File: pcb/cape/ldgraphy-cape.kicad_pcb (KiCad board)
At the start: 2 copper layers, 35.1 x 49.5 mm, 27 parts, among them J1 CONN_01X03, P2 PhDiode, P3 Jumper, P4 BaseConn, P5 CONN_01X05, P6 12V-in, P9 BB_P9, U1 POLOLUSTEPPER, U2 DCDC1584, U3 MIC920, U4 MIC920

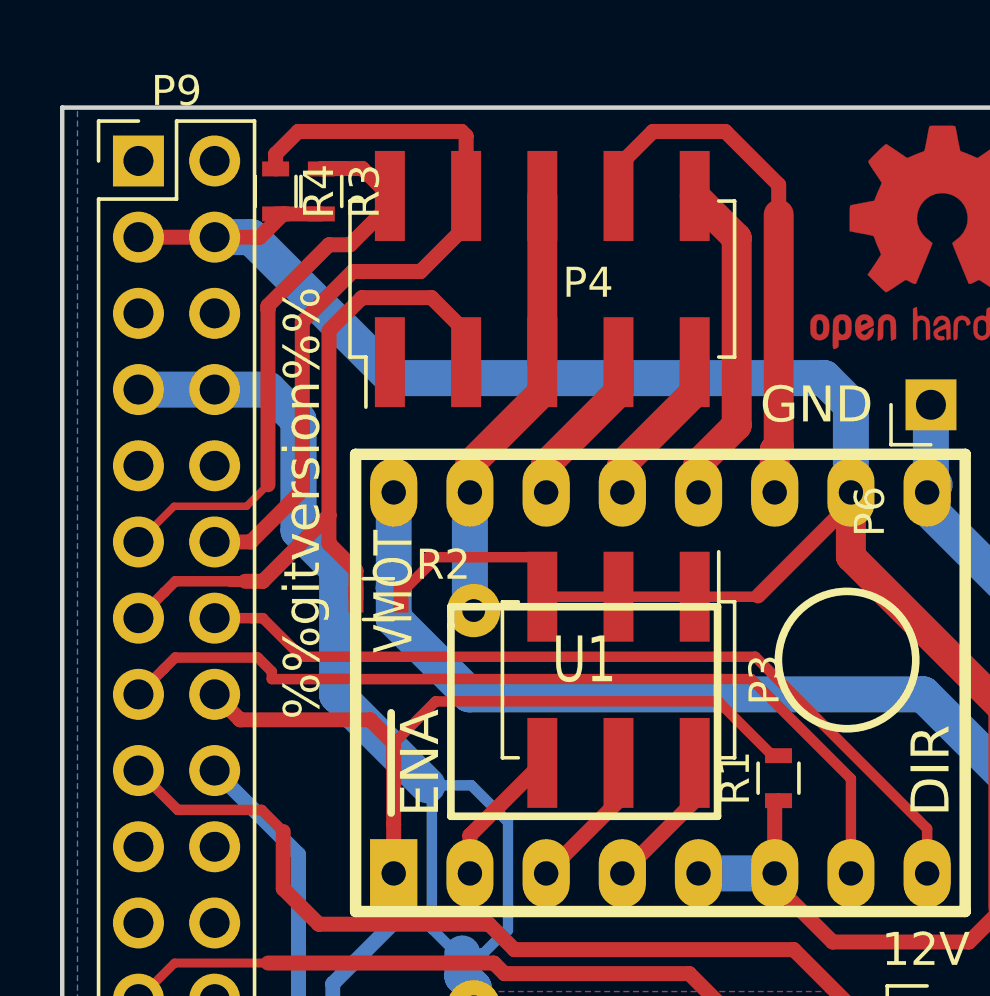
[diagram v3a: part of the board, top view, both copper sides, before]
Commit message: o Update values in schematics.
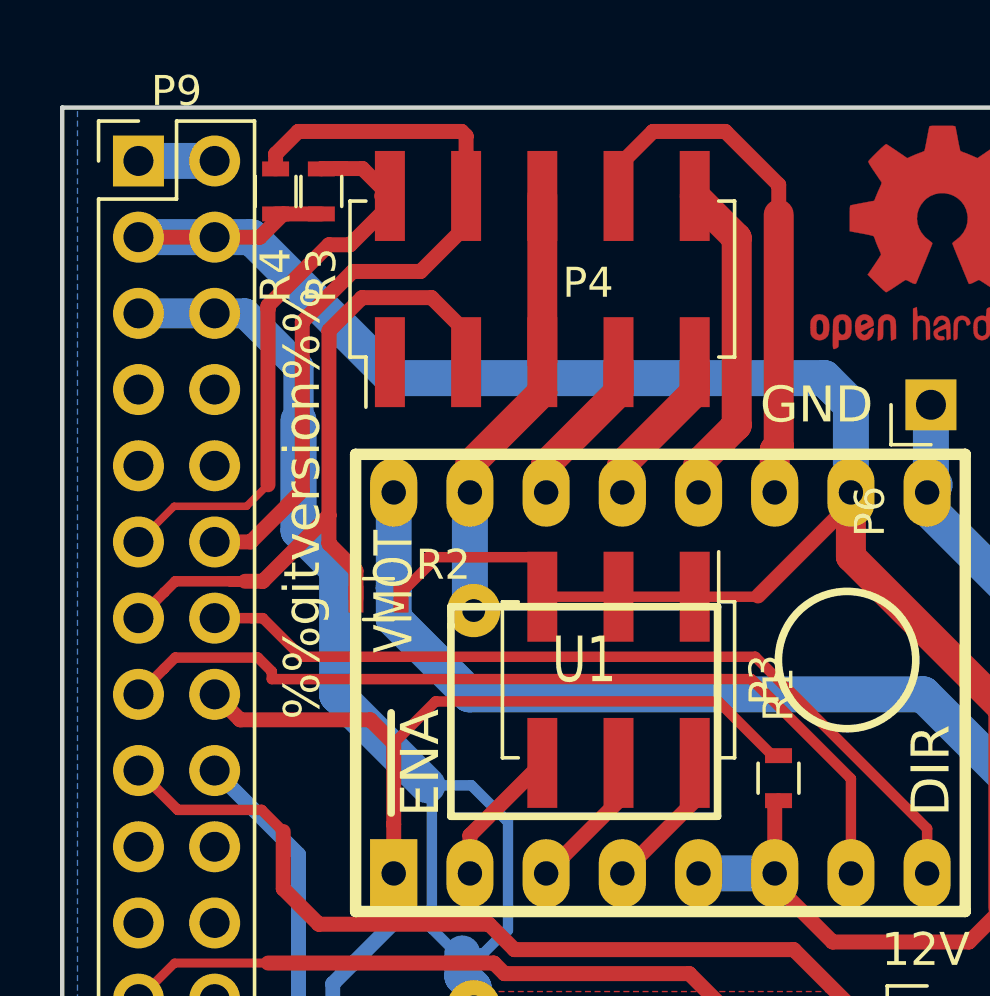
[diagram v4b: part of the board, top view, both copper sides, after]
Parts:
- R10, R13, R15: value R -> 8k2
- R11, R14, R9: value R -> 22k
- R12: value 1k -> 1k5
- R16: value 2k2 -> 8k2
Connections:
- P9 pad 5: (no net) -> +5V
- P9 pad 6: (no net) -> +5V
- P9 pad 7: +5V -> (no net)
- P9 pad 8: +5V -> (no net)
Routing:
- net GND: track 50.1 -> 52.6 mm
- net 3.3V: track 82.5 -> 85.1 mm
- net +5V: track 57.2 -> 59.3 mm
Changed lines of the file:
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@@
   (general
     (links 74)
-    (no_connects 0)
+    (no_connects 2)
     (area 69.774999 41.3705 114.004286 102.945001)
     (thickness 1.6)
     (drawings 17)
-    (tracks 278)
+    (tracks 281)
     (zones 0)
     (modules 27)
@@
     (pad 1 smd rect (at -2.77 -2.54 270) (size 3 1) (layers F.Cu F.Paste F.Mask)
       (net 5 3.3V))
-    (model ${KISYS3DMOD}/Pin_Headers.3dshapes/Pin_Header_Straight_2x03_Pitch2.54mm_SMD.wrl
-      (at (xyz 0 0 0))
-      (scale (xyz 1 1 1))
-      (rotate (xyz 0 0 0))
-    )
   )
   (module TO_SOT_Packages_SMD:SOT-353_SC-70-5 (layer F.Cu)
@@
     (pad 1 smd rect (at -0.95 -0.65 90) (size 0.65 0.4) (layers F.Cu F.Paste F.Mask)
       (net 15 "Net-(R13-Pad1)"))
-    (model ${KISYS3DMOD}/TO_SOT_Packages_SMD.3dshapes/SOT-353_SC-70-5.wrl
+    (model ${KISYS3DMOD}/TO_SOT_Packages_SMD.3dshapes/SC-70-5.wrl
       (at (xyz 0 0 0))
       (scale (xyz 1 1 1))
-      (rotate (xyz 0 0 0))
+      (rotate (xyz 0 0 90))
     )
   )
@@
     (pad 1 smd rect (at -0.95 -0.65 90) (size 0.65 0.4) (layers F.Cu F.Paste F.Mask)
       (net 16 "Net-(R10-Pad2)"))
-    (model ${KISYS3DMOD}/TO_SOT_Packages_SMD.3dshapes/SOT-353_SC-70-5.wrl
+    (model ${KISYS3DMOD}/TO_SOT_Packages_SMD.3dshapes/SC-70-5.wrl
       (at (xyz 0 0 0))
       (scale (xyz 1 1 1))
-      (rotate (xyz 0 0 0))
+      (rotate (xyz 0 0 90))
     )
   )
@@
       (effects (font (size 1 1) (thickness 0.15)))
     )
-    (fp_text value R (at 0 1.5 270) (layer F.Fab)
+    (fp_text value 22k (at 0 1.5 270) (layer F.Fab)
       (effects (font (size 1 1) (thickness 0.15)))
     )
@@
       (effects (font (size 1 1) (thickness 0.15)))
     )
-    (fp_text value R (at 0 1.5 270) (layer F.Fab)
+    (fp_text value 8k2 (at 0 1.5 270) (layer F.Fab)
       (effects (font (size 1 1) (thickness 0.15)))
     )
@@
       (effects (font (size 1 1) (thickness 0.15)))
     )
-    (fp_text value R (at 0 1.5 270) (layer F.Fab)
+    (fp_text value 22k (at 0 1.5 270) (layer F.Fab)
       (effects (font (size 1 1) (thickness 0.15)))
     )
@@
       (effects (font (size 1 1) (thickness 0.15)))
     )
-    (fp_text value 1k (at 0 1.5 90) (layer F.Fab)
+    (fp_text value 1k5 (at 0 1.5 90) (layer F.Fab)
       (effects (font (size 1 1) (thickness 0.15)))
     )
@@
       (effects (font (size 1 1) (thickness 0.15)))
     )
-    (fp_text value R (at 0 1.5 270) (layer F.Fab)
+    (fp_text value 8k2 (at 0 1.5 270) (layer F.Fab)
       (effects (font (size 1 1) (thickness 0.15)))
     )
@@
       (effects (font (size 1 1) (thickness 0.15)))
     )
-    (fp_text value R (at 0 1.5 270) (layer F.Fab)
+    (fp_text value 22k (at 0 1.5 270) (layer F.Fab)
       (effects (font (size 1 1) (thickness 0.15)))
     )
@@
       (effects (font (size 1 1) (thickness 0.15)))
     )
-    (fp_text value R (at 0 1.5 270) (layer F.Fab)
+    (fp_text value 8k2 (at 0 1.5 270) (layer F.Fab)
       (effects (font (size 1 1) (thickness 0.15)))
     )
@@
       (effects (font (size 1 1) (thickness 0.15)))
     )
-    (fp_text value 2k2 (at 0 1.5 180) (layer F.Fab)
+    (fp_text value 8k2 (at 0 1.5 180) (layer F.Fab)
       (effects (font (size 1 1) (thickness 0.15)))
     )
@@
     (tags "resistor 0603")
     (attr smd)
-    (fp_text reference R1 (at 0 -1.45 90) (layer F.SilkS)
+    (fp_text reference R1 (at 2.794 0 90) (layer F.SilkS)
       (effects (font (size 1 1) (thickness 0.15)))
     )
@@
     (tags "resistor 0603")
     (attr smd)
-    (fp_text reference R3 (at 0 -1.45 270) (layer F.SilkS)
+    (fp_text reference R3 (at 2.794 0 270) (layer F.SilkS)
       (effects (font (size 1 1) (thickness 0.15)))
     )
@@
       (net 25 ~UI-Button))
     (pad 1 smd rect (at -2.77 -5.08 90) (size 3 1) (layers F.Cu F.Paste F.Mask))
-    (model ${KISYS3DMOD}/Pin_Headers.3dshapes/Pin_Header_Straight_2x05_Pitch2.54mm_SMD.wrl
+    (model ${KISYS3DMOD}/Pin_Headers.3dshapes/Pin_Header_Straight_2x05_Pitch2.54mm.wrl
       (at (xyz 0 0 0))
       (scale (xyz 1 1 1))
-      (rotate (xyz 0 0 0))
+      (rotate (xyz 0 0 90))
     )
   )
@@
     (tags "resistor 0603")
     (attr smd)
-    (fp_text reference R4 (at 0 -1.45 270) (layer F.SilkS)
+    (fp_text reference R4 (at 2.794 0 270) (layer F.SilkS)
       (effects (font (size 1 1) (thickness 0.15)))
     )
@@
     (pad 10 thru_hole oval (at 2.54 10.16) (size 1.7 1.7) (drill 1) (layers *.Cu *.Mask))
     (pad 9 thru_hole oval (at 0 10.16) (size 1.7 1.7) (drill 1) (layers *.Cu *.Mask))
-    (pad 8 thru_hole oval (at 2.54 7.62) (size 1.7 1.7) (drill 1) (layers *.Cu *.Mask)
+    (pad 8 thru_hole oval (at 2.54 7.62) (size 1.7 1.7) (drill 1) (layers *.Cu *.Mask))
+    (pad 7 thru_hole oval (at 0 7.62) (size 1.7 1.7) (drill 1) (layers *.Cu *.Mask))
+    (pad 6 thru_hole oval (at 2.54 5.08) (size 1.7 1.7) (drill 1) (layers *.Cu *.Mask)
       (net 8 +5V))
-    (pad 7 thru_hole oval (at 0 7.62) (size 1.7 1.7) (drill 1) (layers *.Cu *.Mask)
+    (pad 5 thru_hole oval (at 0 5.08) (size 1.7 1.7) (drill 1) (layers *.Cu *.Mask)
       (net 8 +5V))
-    (pad 6 thru_hole oval (at 2.54 5.08) (size 1.7 1.7) (drill 1) (layers *.Cu *.Mask))
-    (pad 5 thru_hole oval (at 0 5.08) (size 1.7 1.7) (drill 1) (layers *.Cu *.Mask))
     (pad 4 thru_hole oval (at 2.54 2.54) (size 1.7 1.7) (drill 1) (layers *.Cu *.Mask)
       (net 5 3.3V))
@@
   (gr_line (start 106.68 43.18) (end 106.68 92.71) (layer Edge.Cuts) (width 0.15))
   (gr_line (start 71.628 43.18) (end 106.68 43.18) (layer Edge.Cuts) (width 0.15))
+  (segment (start 76.708 44.958) (end 74.168 44.958) (width 1.2) (layer B.Cu) (net 1))
   (segment (start 85.217 56.007) (end 85.217 59.817) (width 1.2) (layer B.Cu) (net 1))
   (segment (start 85.217 59.817) (end 85.344 59.944) (width 1.2) (layer B.Cu) (net 1))
@@
   (segment (start 81.161 86.36) (end 79.502 84.701) (width 0.5) (layer B.Cu) (net 4))
   (segment (start 82.5246 86.36) (end 82.677 86.36) (width 0.35) (layer F.Cu) (net 4))
+  (segment (start 76.708 47.498) (end 74.168 47.498) (width 1.2) (layer B.Cu) (net 5))
   (segment (start 97.917 56.007) (end 97.917 58.15) (width 1) (layer F.Cu) (net 5))
   (segment (start 97.917 58.15) (end 102.997 63.23) (width 1) (layer F.Cu) (net 5))
@@
   (segment (start 100.457 67.214) (end 94.728001 61.485001) (width 0.35) (layer F.Cu) (net 7))
   (segment (start 100.457 68.707) (end 100.457 67.214) (width 0.35) (layer F.Cu) (net 7))
+  (segment (start 76.708 50.038) (end 74.168 50.038) (width 1) (layer B.Cu) (net 8))
+  (segment (start 77.724 50.038) (end 76.708 50.038) (width 1) (layer B.Cu) (net 8))
+  (segment (start 79.502 51.816) (end 77.724 50.038) (width 1) (layer B.Cu) (net 8))
+  (segment (start 79.502 53.594) (end 79.502 51.816) (width 1) (layer B.Cu) (net 8))
   (segment (start 85.344 73.152) (end 85.344 74.409235) (width 1.2) (layer F.Cu) (net 8))
   (segment (start 85.344 74.409235) (end 87.274508 76.339743) (width 1.2) (layer F.Cu) (net 8))
@@
   (segment (start 83.804401 65.770401) (end 84.265754 65.770401) (width 0.35) (layer B.Cu) (net 8))
   (segment (start 84.963 72.136) (end 84.963 71.374) (width 1.2) (layer B.Cu) (net 8))
-  (segment (start 76.708 52.578) (end 74.168 52.578) (width 1.2) (layer B.Cu) (net 8))
   (segment (start 83.804401 65.770401) (end 80.78959 62.75559) (width 1.2) (layer B.Cu) (net 8))
-  (segment (start 79.502 53.594) (end 78.486 52.578) (width 1.2) (layer B.Cu) (net 8))
   (segment (start 80.78959 62.75559) (end 80.78959 58.56459) (width 1.2) (layer B.Cu) (net 8))
   (segment (start 80.78959 58.56459) (end 79.502 57.277) (width 1.2) (layer B.Cu) (net 8))
   (segment (start 79.502 57.277) (end 79.502 53.594) (width 1.2) (layer B.Cu) (net 8))
-  (segment (start 78.486 52.578) (end 76.708 52.578) (width 1.2) (layer B.Cu) (net 8))
   (segment (start 88.60854 76.479508) (end 87.274508 76.479508) (width 1.2) (layer F.Cu) (net 8))
   (segment (start 87.59254 77.520508) (end 87.59254 82.296508) (width 0.5) (layer F.Cu) (net 8))

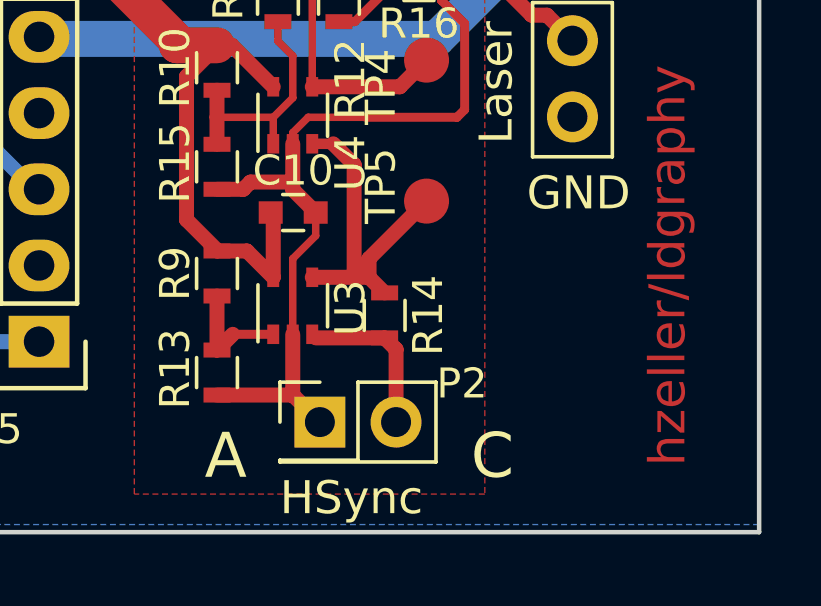
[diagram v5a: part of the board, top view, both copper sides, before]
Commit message: Add photo diode compensating cap in feedback loop.
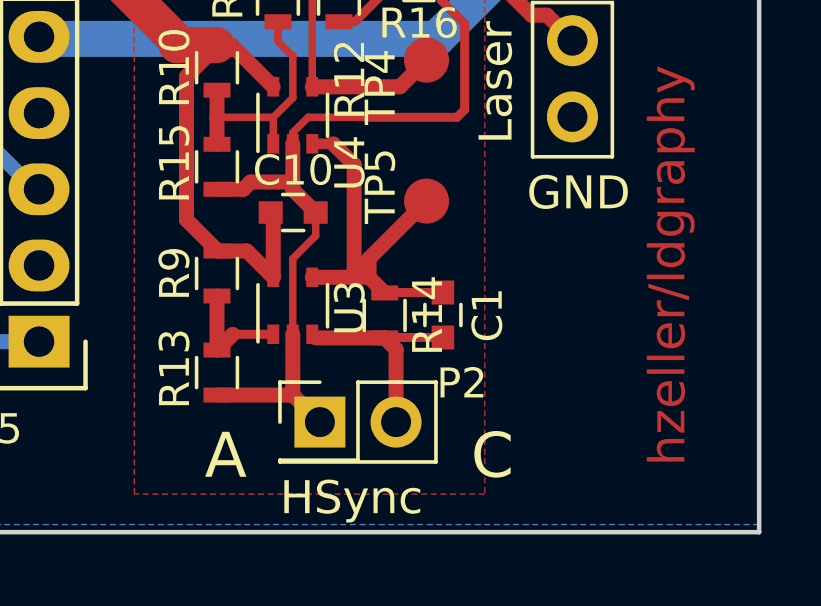
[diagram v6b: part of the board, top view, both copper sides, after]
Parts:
- added C1: C, Capacitors_SMD:C_0603, F.Cu at (96.1, 85.5)
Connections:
- P4 pad 1: (no net) -> Net-(P4-Pad1)
- P5 pad 2: (no net) -> Net-(P5-Pad2)
- P9 pad 10: (no net) -> Net-(P9-Pad10)
- P9 pad 19: (no net) -> Net-(P9-Pad19)
- P9 pad 20: (no net) -> Net-(P9-Pad20)
- P9 pad 21: (no net) -> Net-(P9-Pad21)
- P9 pad 22: (no net) -> Net-(P9-Pad22)
- P9 pad 24: (no net) -> Net-(P9-Pad24)
- P9 pad 25: (no net) -> Net-(P9-Pad25)
- P9 pad 26: (no net) -> Net-(P9-Pad26)
- P9 pad 27: (no net) -> Net-(P9-Pad27)
- P9 pad 28: (no net) -> Net-(P9-Pad28)
- P9 pad 29: (no net) -> Net-(P9-Pad29)
- P9 pad 30: (no net) -> Net-(P9-Pad30)
- P9 pad 31: (no net) -> Net-(P9-Pad31)
- P9 pad 32: (no net) -> Net-(P9-Pad32)
- P9 pad 33: (no net) -> Net-(P9-Pad33)
- P9 pad 34: (no net) -> Net-(P9-Pad34)
- P9 pad 35: (no net) -> Net-(P9-Pad35)
- P9 pad 36: (no net) -> Net-(P9-Pad36)
- P9 pad 7: (no net) -> Net-(P9-Pad7)
- P9 pad 8: (no net) -> Net-(P9-Pad8)
- P9 pad 9: (no net) -> Net-(P9-Pad9)
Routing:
- net /VPhoto: track 11.4 -> 13.3 mm
- net Net-(C1-Pad2): track 5.26 -> 7.20 mm
